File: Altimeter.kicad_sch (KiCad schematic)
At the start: 54 parts, among them IC1 XTSD02GLGEAG, J1 Conn_01x04_Male, J2 Conn_01x02_Male, Q1 PMV20ENR, U1 150044M155220, U2 ESP32-S3, U4 DPS310, Y1 40MHz±10ppm

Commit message: started making it thinner but realised it could be even thinner
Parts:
- added TP16, TP17, TP18, TP19: TestPoint, TestPoint:TestPoint_Pad_D1.0mm, symbol Connector:TestPoint
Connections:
- net Accel/Gyro: now also U2.43 (GPIO38); no longer U2.44 (MTCK/JTAG/GPIO39)
- net Buzzer: now also U2.36 (SPICLK_N/GPIO48); no longer U2.43 (GPIO38)
- net RXD: now also U2.50 (U0RXD/PROG/GPIO44); no longer U2.47 (MTDI/JTAG/GPIO41)
- net at U2.48 (MTMS/JTAG/GPIO42): now also TP19.1; no longer R9.2
- net at U2.45 (MTDO/JTAG/GPIO40): now also TP17.1
- net at U2.49 (U0TXD/PROG/GPIO43): now also R9.2
- new net: TP16.1, U2.44 (MTCK/JTAG/GPIO39)
- new net: TP18.1, U2.47 (MTDI/JTAG/GPIO41)
- no-connect marks 25 -> 21
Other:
- moved on the sheet: R9
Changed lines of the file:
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@@
   (junction (at 16.51 101.6) (diameter 0) (color 0 0 0 0)
   )
-  (junction (at 53.34 127) (diameter 0) (color 0 0 0 0)
-  )
   (junction (at 30.48 191.77) (diameter 0) (color 0 0 0 0)
   )
@@
   (junction (at 15.24 111.76) (diameter 0) (color 0 0 0 0)
   )
+  (junction (at 50.8 127) (diameter 0) (color 0 0 0 0)
+  )
   (junction (at 167.64 132.08) (diameter 0) (color 0 0 0 0)
   )
@@
   )
   (no_connect (at 69.85 90.17))
-  (no_connect (at 69.85 113.03))
-  (no_connect (at 69.85 115.57))
   (no_connect (at 43.18 101.6))
   (no_connect (at 69.85 92.71))
@@
   (no_connect (at 135.89 130.81))
   (no_connect (at 135.89 72.39))
-  (no_connect (at 69.85 120.65))
-  (no_connect (at 135.89 115.57))
   (no_connect (at 135.89 113.03))
   (no_connect (at 135.89 82.55))
@@
     (stroke (width 0) (type default))
   )
-  (wire (pts (xy 67.31 118.11) (xy 69.85 118.11))
-    (stroke (width 0) (type default))
-  )
   (polyline (pts (xy 68.58 76.2) (xy 68.58 78.74))
     (stroke (width 0) (type default))
@@
     (stroke (width 0) (type default))
   )
+  (wire (pts (xy 68.58 113.03) (xy 69.85 113.03))
+    (stroke (width 0) (type default))
+  )
   (wire (pts (xy 52.07 97.79) (xy 52.07 106.68))
     (stroke (width 0) (type default))
@@
     (stroke (width 0) (type default))
   )
-  (wire (pts (xy 60.96 125.73) (xy 62.23 125.73))
-    (stroke (width 0) (type default))
-  )
-  (wire (pts (xy 50.8 127) (xy 53.34 127))
-    (stroke (width 0) (type default))
-  )
   (wire (pts (xy 213.36 96.52) (xy 233.68 96.52))
     (stroke (width 0) (type default))
@@
     (stroke (width 0) (type default))
   )
-  (wire (pts (xy 135.89 107.95) (xy 138.43 107.95))
-    (stroke (width 0) (type default))
-  )
   (wire (pts (xy 201.93 80.01) (xy 233.68 80.01))
     (stroke (width 0) (type default))
@@
     (stroke (width 0) (type default))
   )
-  (wire (pts (xy 53.34 127) (xy 55.88 127))
+  (wire (pts (xy 50.8 127) (xy 55.88 127))
     (stroke (width 0) (type default))
   )
@@
   )
   (wire (pts (xy 163.83 90.17) (xy 163.83 87.63))
-    (stroke (width 0) (type default))
-  )
-  (wire (pts (xy 68.58 125.73) (xy 69.85 125.73))
     (stroke (width 0) (type default))
   )
@@
     (effects (font (size 1.27 1.27)) (justify left bottom))
   )
-  (label "TXD" (at 62.23 125.73 180) (fields_autoplaced)
+  (label "TXD" (at 60.96 113.03 180) (fields_autoplaced)
     (effects (font (size 1.27 1.27)) (justify right bottom))
   )
@@
     (effects (font (size 1.27 1.27)) (justify right bottom))
   )
-  (label "Accel{slash}Gyro" (at 67.31 118.11 180) (fields_autoplaced)
-    (effects (font (size 1.27 1.27)) (justify right bottom))
-  )
-  (label "RXD" (at 69.85 123.19 180) (fields_autoplaced)
+  (label "Accel{slash}Gyro" (at 135.89 107.95 0) (fields_autoplaced)
+    (effects (font (size 1.27 1.27)) (justify left bottom))
+  )
+  (label "RXD" (at 69.85 115.57 180) (fields_autoplaced)
     (effects (font (size 1.27 1.27)) (justify right bottom))
   )
@@
     (effects (font (size 1.27 1.27)) (justify left bottom))
   )
-  (label "Buzzer" (at 138.43 107.95 0) (fields_autoplaced)
+  (label "Buzzer" (at 135.89 115.57 0) (fields_autoplaced)
     (effects (font (size 1.27 1.27)) (justify left bottom))
   )
@@
         (path "/7db990e4-92e1-4f99-b4d2-435bbec1ba83"
           (reference "#PWR07") (unit 1)
+        )
+      )
+    )
+  )
+  (symbol (lib_id "Connector:TestPoint") (at 69.85 125.73 90) (unit 1)
+    (in_bom yes) (on_board yes) (dnp no)
+    (property "Reference" "TP19" (at 60.96 125.73 90)
+      (effects (font (size 1.27 1.27)) (justify right))
+    )
+    (property "Value" "TestPoint" (at 52.07 125.73 90)
+      (effects (font (size 1.27 1.27)) (justify right))
+    )
+    (property "Footprint" "TestPoint:TestPoint_Pad_D1.0mm" (at 69.85 120.65 0)
+      (effects (font (size 1.27 1.27)) hide)
+    )
+    (property "Datasheet" "~" (at 69.85 120.65 0)
+      (effects (font (size 1.27 1.27)) hide)
+    )
+    (pin "1")
+    (instances
+      (project "Altimeter"
+        (path "/7db990e4-92e1-4f99-b4d2-435bbec1ba83"
+          (reference "TP19") (unit 1)
+        )
+      )
+    )
+  )
+  (symbol (lib_id "Connector:TestPoint") (at 69.85 120.65 90) (unit 1)
+    (in_bom yes) (on_board yes) (dnp no)
+    (property "Reference" "TP17" (at 60.96 120.65 90)
+      (effects (font (size 1.27 1.27)) (justify right))
+    )
+    (property "Value" "TestPoint" (at 52.07 120.65 90)
+      (effects (font (size 1.27 1.27)) (justify right))
+    )
+    (property "Footprint" "TestPoint:TestPoint_Pad_D1.0mm" (at 69.85 115.57 0)
+      (effects (font (size 1.27 1.27)) hide)
+    )
+    (property "Datasheet" "~" (at 69.85 115.57 0)
+      (effects (font (size 1.27 1.27)) hide)
+    )
+    (pin "1")
+    (instances
+      (project "Altimeter"
+        (path "/7db990e4-92e1-4f99-b4d2-435bbec1ba83"
+          (reference "TP17") (unit 1)
         )
       )
@@
     )
   )
-  (symbol (lib_id "power:+3.3V") (at 53.34 127 0) (unit 1)
-    (in_bom yes) (on_board yes) (dnp no)
-    (property "Reference" "#PWR013" (at 53.34 130.81 0)
-      (effects (font (size 1.27 1.27)) hide)
-    )
-    (property "Value" "+3.3V" (at 53.721 122.6058 0)
-      (effects (font (size 1.27 1.27)))
-    )
-    (property "Footprint" "" (at 53.34 127 0)
-      (effects (font (size 1.27 1.27)) hide)
-    )
-    (property "Datasheet" "" (at 53.34 127 0)
+  (symbol (lib_id "power:+3.3V") (at 50.8 127 0) (unit 1)
+    (in_bom yes) (on_board yes) (dnp no)
+    (property "Reference" "#PWR013" (at 50.8 130.81 0)
+      (effects (font (size 1.27 1.27)) hide)
+    )
+    (property "Value" "+3.3V" (at 48.26 123.19 0)
+      (effects (font (size 1.27 1.27)))
+    )
+    (property "Footprint" "" (at 50.8 127 0)
+      (effects (font (size 1.27 1.27)) hide)
+    )
+    (property "Datasheet" "" (at 50.8 127 0)
       (effects (font (size 1.27 1.27)) hide)
     )
@@
         (path "/7db990e4-92e1-4f99-b4d2-435bbec1ba83"
           (reference "TP7") (unit 1)
+        )
+      )
+    )
+  )
+  (symbol (lib_id "Connector:TestPoint") (at 69.85 118.11 90) (unit 1)
+    (in_bom yes) (on_board yes) (dnp no)
+    (property "Reference" "TP16" (at 60.96 118.11 90)
+      (effects (font (size 1.27 1.27)) (justify right))
+    )
+    (property "Value" "TestPoint" (at 52.07 118.11 90)
+      (effects (font (size 1.27 1.27)) (justify right))
+    )
+    (property "Footprint" "TestPoint:TestPoint_Pad_D1.0mm" (at 69.85 113.03 0)
+      (effects (font (size 1.27 1.27)) hide)
+    )
+    (property "Datasheet" "~" (at 69.85 113.03 0)
+      (effects (font (size 1.27 1.27)) hide)
+    )
+    (pin "1")
+    (instances
+      (project "Altimeter"
+        (path "/7db990e4-92e1-4f99-b4d2-435bbec1ba83"
+          (reference "TP16") (unit 1)
         )
       )
@@
     )
   )
-  (symbol (lib_id "Device:R") (at 64.77 125.73 90) (unit 1)
-    (in_bom yes) (on_board yes) (dnp no)
-    (property "Reference" "R9" (at 63.5 123.19 90)
-      (effects (font (size 1.27 1.27)))
-    )
-    (property "Value" "499" (at 59.69 123.19 90)
-      (effects (font (size 1.27 1.27)))
-    )
-    (property "Footprint" "Resistor_SMD:R_0402_1005Metric" (at 64.77 127.508 90)
-      (effects (font (size 1.27 1.27)) hide)
-    )
-    (property "Datasheet" "~" (at 64.77 125.73 0)
+  (symbol (lib_id "Device:R") (at 64.77 113.03 90) (unit 1)
+    (in_bom yes) (on_board yes) (dnp no)
+    (property "Reference" "R9" (at 63.5 110.49 90)
+      (effects (font (size 1.27 1.27)))
+    )
+    (property "Value" "499" (at 59.69 110.49 90)
+      (effects (font (size 1.27 1.27)))
+    )
+    (property "Footprint" "Resistor_SMD:R_0402_1005Metric" (at 64.77 114.808 90)
+      (effects (font (size 1.27 1.27)) hide)
+    )
+    (property "Datasheet" "~" (at 64.77 113.03 0)
       (effects (font (size 1.27 1.27)) hide)
     )
@@
         )
       )
+    )
+  )
+  (symbol (lib_id "Connector:TestPoint") (at 69.85 123.19 90) (unit 1)
+    (in_bom yes) (on_board yes) (dnp no)
+    (property "Reference" "TP18" (at 60.96 123.19 90)
+      (effects (font (size 1.27 1.27)) (justify right))
+    )
+    (property "Value" "TestPoint" (at 52.07 123.19 90)
+      (effects (font (size 1.27 1.27)) (justify right))
+    )
+    (property "Footprint" "TestPoint:TestPoint_Pad_D1.0mm" (at 69.85 118.11 0)
+      (effects (font (size 1.27 1.27)) hide)
+    )
+    (property "Datasheet" "~" (at 69.85 118.11 0)
+      (effects (font (size 1.27 1.27)) hide)
+    )
+    (pin "1")
+    (instances
+      (project "Altimeter"
+        (path "/7db990e4-92e1-4f99-b4d2-435bbec1ba83"
+          (reference "TP18") (unit 1)
+        )
+      )

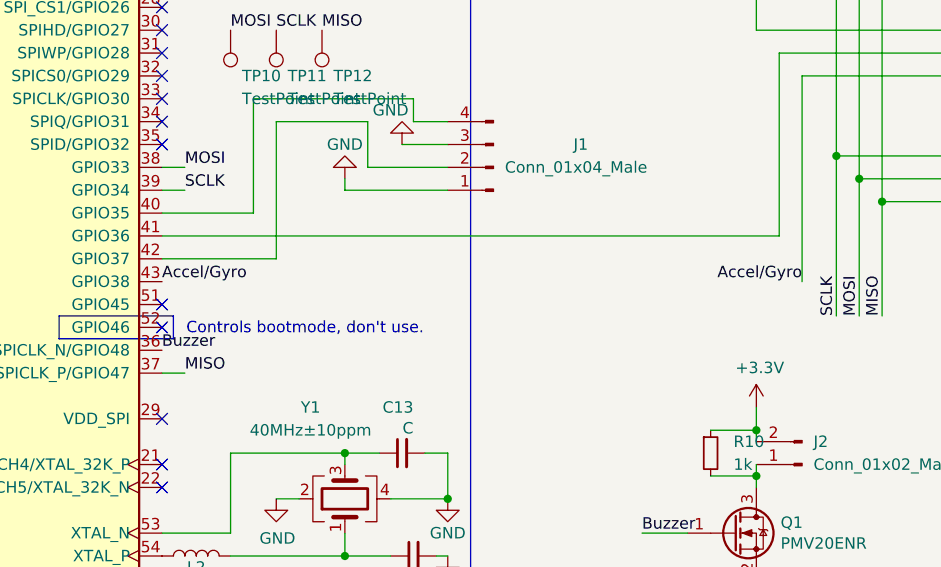
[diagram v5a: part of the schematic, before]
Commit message: spaced out vias and changed j4
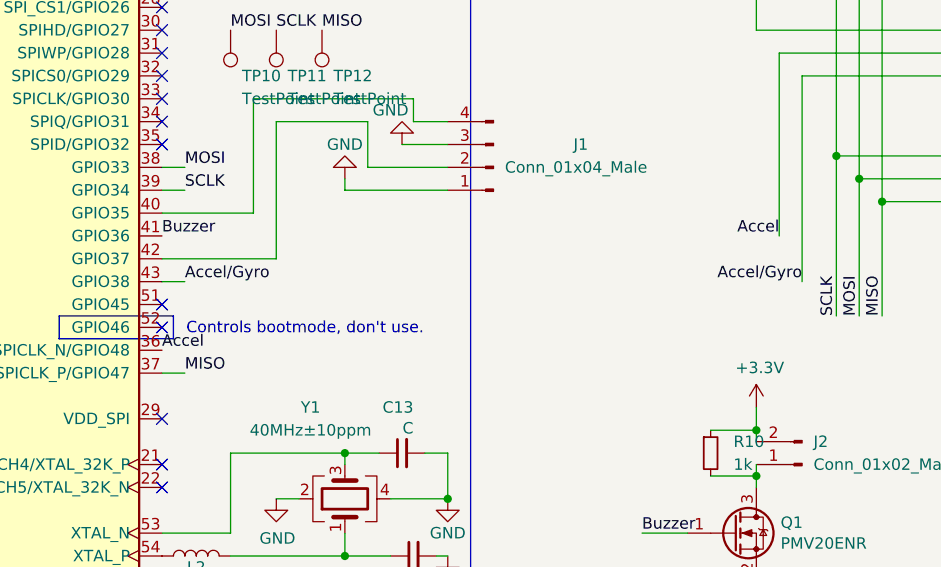
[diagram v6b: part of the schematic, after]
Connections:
- net IMU/Accelerometer is gone; now on net Buzzer: U2.41 (GPIO36)
- net Buzzer: no longer U2.36 (SPICLK_N/GPIO48)
- new net Accel: U2.36 (SPICLK_N/GPIO48)
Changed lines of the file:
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@@
-    (stroke (width 0) (type default))
-  )
-  (wire (pts (xy 135.89 102.87) (xy 204.47 102.87))
     (stroke (width 0) (type default))
   )
@@
   )
   (wire (pts (xy 201.93 124.46) (xy 201.93 125.73))
+    (stroke (width 0) (type default))
+  )
+  (wire (pts (xy 138.43 107.95) (xy 135.89 107.95))
     (stroke (width 0) (type default))
   )
@@
     (effects (font (size 1.27 1.27)) (justify right bottom))
   )
-  (label "Accel{slash}Gyro" (at 135.89 107.95 0) (fields_autoplaced)
+  (label "Accel{slash}Gyro" (at 138.43 107.95 0) (fields_autoplaced)
     (effects (font (size 1.27 1.27)) (justify left bottom))
   )
@@
     (effects (font (size 1.27 1.27)) (justify left bottom))
   )
+  (label "Accel" (at 135.89 115.57 0) (fields_autoplaced)
+    (effects (font (size 1.27 1.27)) (justify left bottom))
+  )
   (label "BOOT" (at 68.58 165.1 180) (fields_autoplaced)
     (effects (font (size 1.27 1.27)) (justify right bottom))
@@
     (effects (font (size 1.27 1.27)) (justify left bottom))
   )
-  (label "Buzzer" (at 135.89 115.57 0) (fields_autoplaced)
+  (label "Buzzer" (at 135.89 102.87 0) (fields_autoplaced)
     (effects (font (size 1.27 1.27)) (justify left bottom))
   )
@@
     (effects (font (size 1.27 1.27)) (justify left bottom))
   )
+  (label "Accel" (at 204.47 102.87 180) (fields_autoplaced)
+    (effects (font (size 1.27 1.27)) (justify right bottom))
+  )
   (label "BattVolt" (at 121.92 35.56 180) (fields_autoplaced)
